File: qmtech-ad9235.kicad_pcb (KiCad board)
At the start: 4 copper layers, 55 x 75 mm, 55 parts

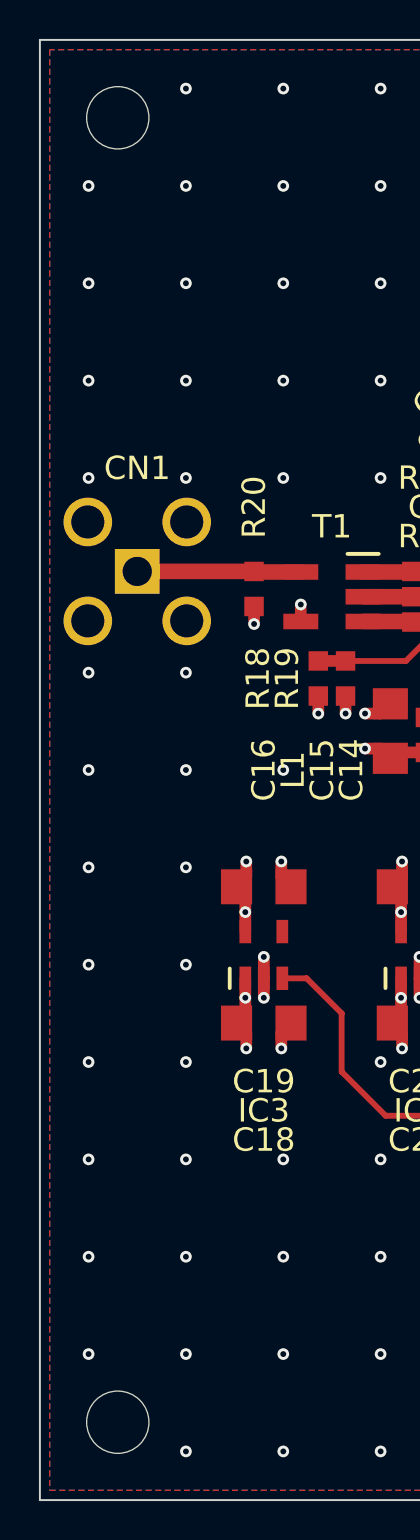
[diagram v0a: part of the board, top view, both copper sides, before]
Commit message: move M3 holes away from edge
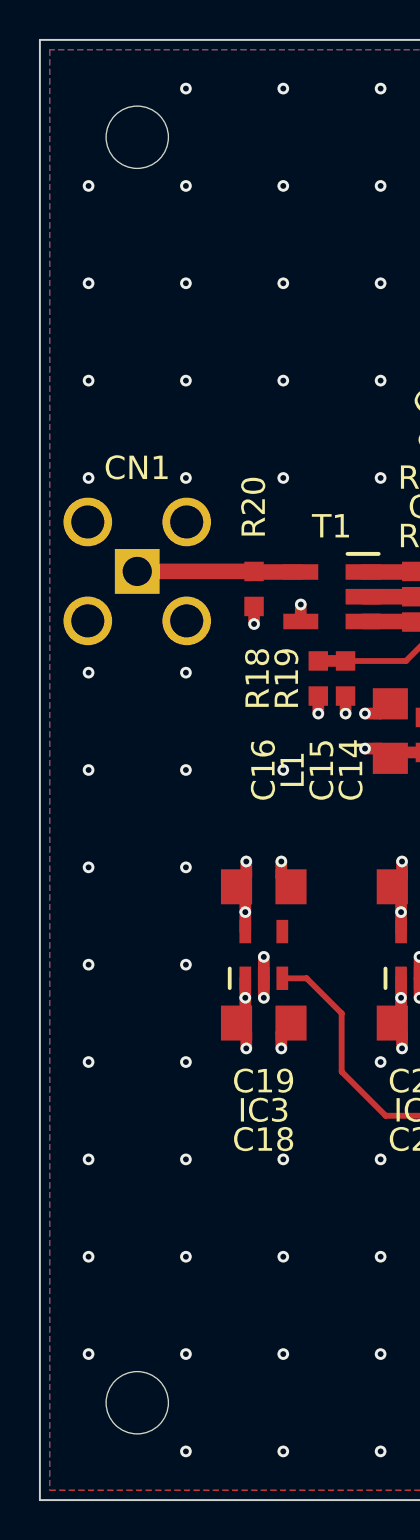
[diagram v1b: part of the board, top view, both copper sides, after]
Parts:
- moved M1 1.41 mm to (125.0, 60.0)
- moved M2 1.41 mm to (125.0, 125.0)
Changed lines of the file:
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@@
   )
   (footprint "footprints:M3" (layer "F.Cu")
-    (at 124 59)
+    (at 125 60)
     (property "mpn" "hole")
     (clearance 1)
@@
   )
   (footprint "footprints:M3" (layer "F.Cu")
-    (at 124 126)
+    (at 125 125)
     (property "mpn" "hole")
     (clearance 1)

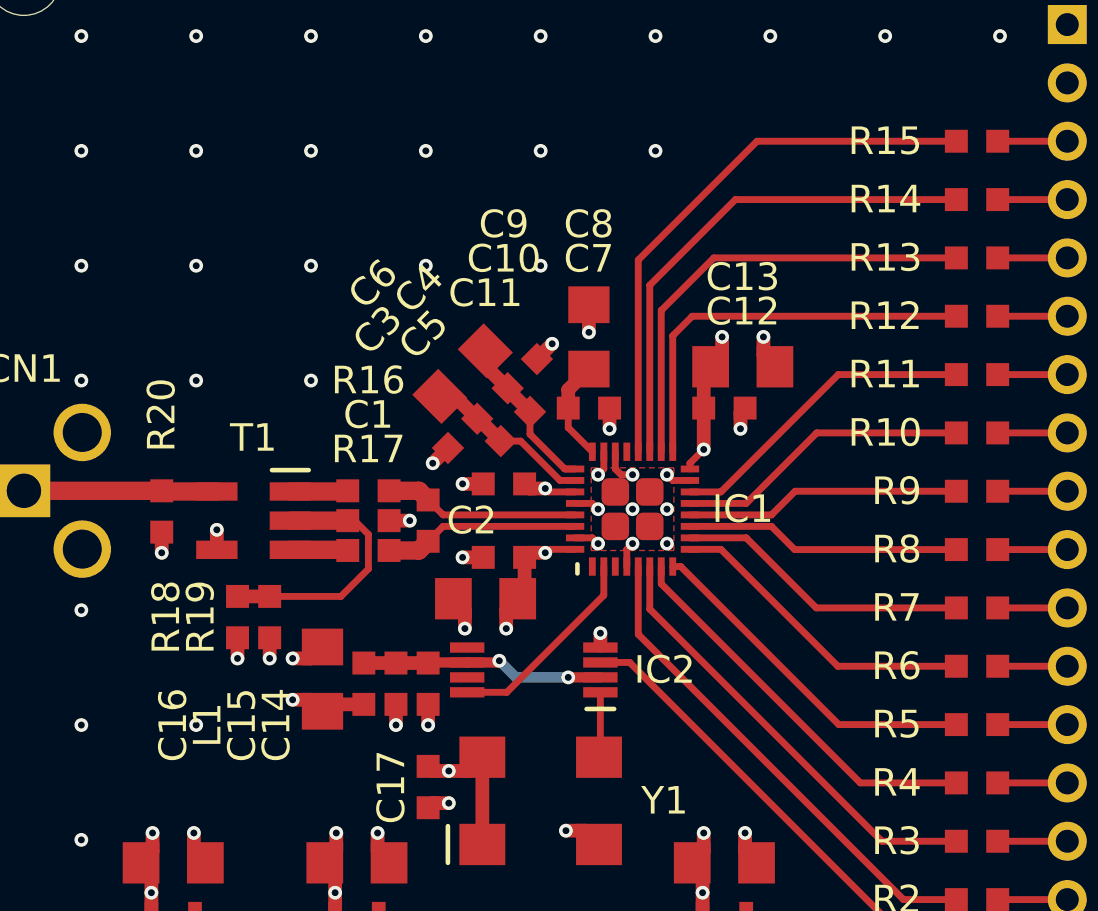
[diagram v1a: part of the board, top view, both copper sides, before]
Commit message: improve DVDD decoupling in qmtech-ad9235
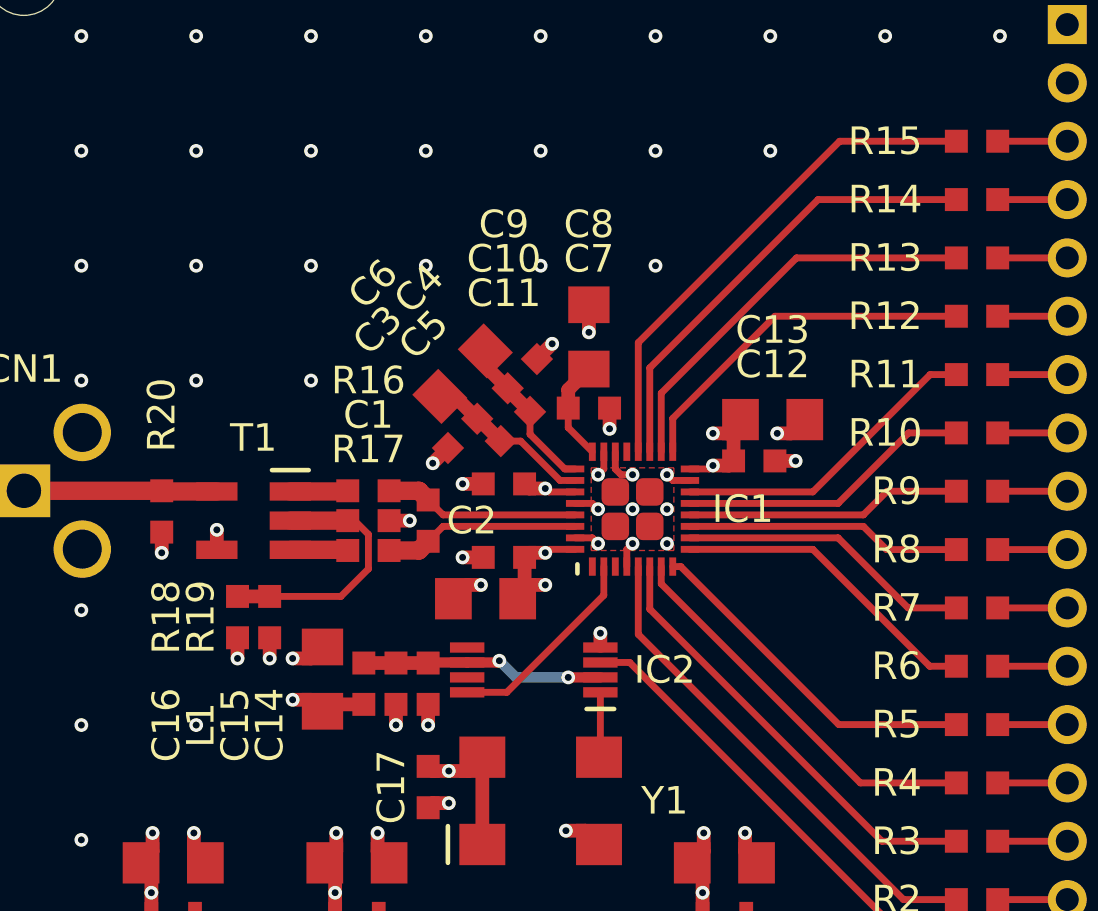
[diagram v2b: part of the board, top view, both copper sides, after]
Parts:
- moved C12 2.64 mm to (156.8, 81.0)
- moved C13 2.64 mm to (157.6, 79.2)
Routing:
- net D12: track 22.1 -> 20.0 mm
- net D13: track 24.3 -> 22.2 mm
- net D10: track 17.8 -> 15.6 mm
- net D11: track 19.9 -> 17.8 mm
- net DVDD: track 10.3 -> 9.41 mm
- net GND: track 42.3 -> 42.1 mm, vias 134 -> 136

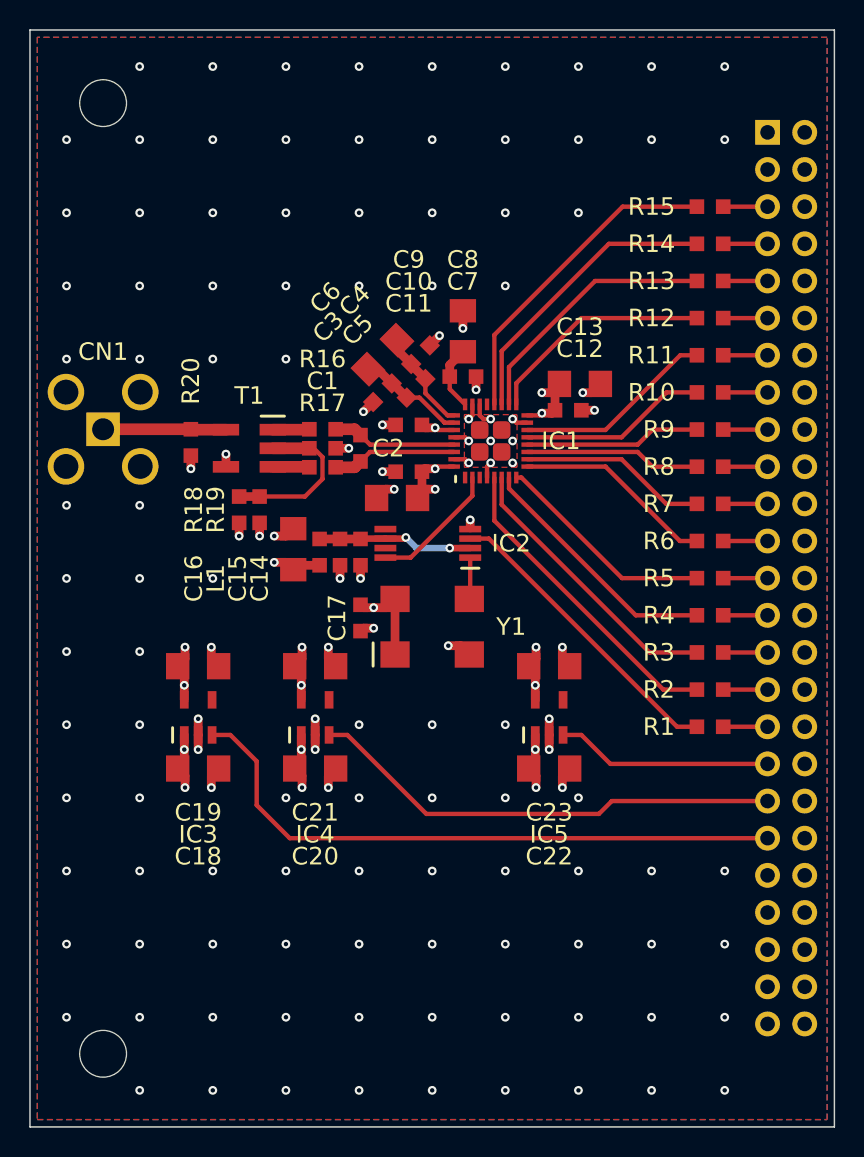
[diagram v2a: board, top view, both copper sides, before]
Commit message: add GND plane cutout around data traces in qmtech-ad9235
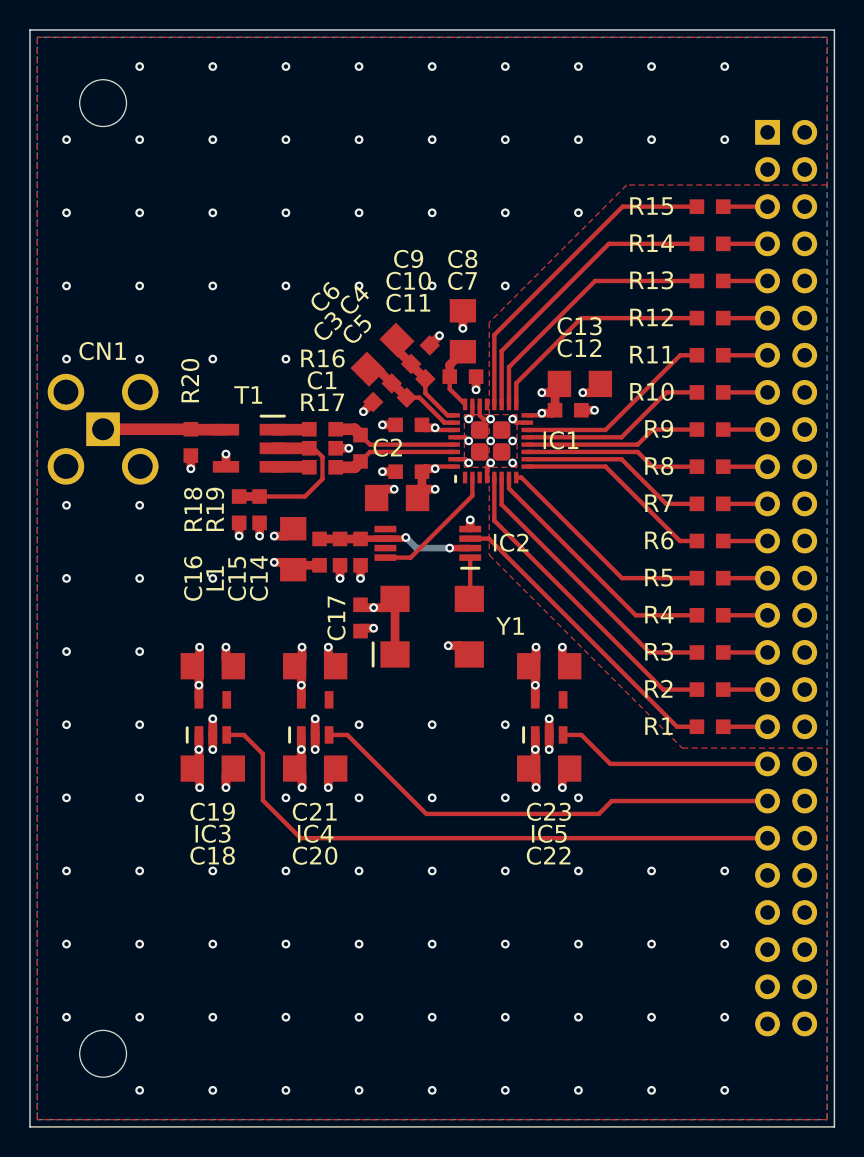
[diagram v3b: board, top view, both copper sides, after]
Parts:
- moved C18 1.00 mm to (132.5, 105.5)
- moved C19 1.00 mm to (132.5, 98.5)
- moved IC3 1.00 mm to (132.5, 102.0)
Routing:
- net AEN: track 42.7 -> 41.8 mm
